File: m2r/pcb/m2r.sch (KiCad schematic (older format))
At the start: 106 parts, among them IC1 ADP3338, IC10 STM32F303C, IC11 TPS76327, IC2 APU1205-HF-3, IC3 ADuM1201, IC4 MS5611-01BA03, IC5 ADuM1201, IC6 ADL5324, IC7 NTX2B, IC8 MAX-7Q, IC9 ALM-2712, P1 CONN_2, P2 CONN_2, P3 CONN_4, P4 RockBLOCK, P5 SWD, P6 SMA, P7 CONN_2, X1 BAT BOX, X2 ARM SW, X3 RG LED, X4 8M

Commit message: add farnell number for new barometer
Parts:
- IC4: Farnell (none) -> 2362662
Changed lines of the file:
@@
 F 2 "" H 4950 1050 60  0000 C CNN
 F 3 "" H 4950 1050 60  0000 C CNN
+F 4 "2362662" H 4950 1050 60  0001 C CNN "Farnell"
 	1    4950 1050
 	1    0    0    -1

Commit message: update farnell codes
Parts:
- IC1: Farnell (none) -> 1651284
- IC10: Farnell (none) -> 2333361
- IC11: Farnell (none) -> 1755502
- IC9: Farnell (none) -> 1865153
- P4: Farnell (none) -> 1756828

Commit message: make a good start on m2d schematic
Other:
- note added: "INTERNAL STATUS LEDS"
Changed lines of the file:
@@
 Wire Wire Line
 	6000 1450 6000 1400
+Text Notes 8400 5450 0    60   ~ 0
+INTERNAL STATUS LEDS
 $EndSCHEMATC

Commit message: further wibbling about things
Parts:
- removed C4: 100n, 0603, symbol C
- removed IC2: APU1205-HF-3, symbol APU1205-HF-3
- removed IC4: MS5611-01BA03, symbol MS5611-01BA03
- removed IC7: NTX2B, symbol NTX2B
- removed R1: 10k, 0603, symbol R
- removed TP19, TP20, TP21, TP22: TESTPAD, symbol TESTPAD
- added IC2: ADP3335, symbol ADP3335
- added IC6: MTX2, symbol MTX2
- added TP13, TP14: TESTPAD, symbol TESTPAD
- renumbered C11 to C10, C12 to C11, C13 to C12, C14 to C13, C15 to C14, C16 to C15, C17 to C16, C18 to C17, C19 to C18, C20 to C19, C21 to C20, C22 to C21, C23 to C22, C24 to C23, C25 to C24, C26 to C25, C27 to C26, C28 to C27, C29 to C28, C30 to C29, C31 to C30, C32 to C31, C33 to C32, C34 to C33, C35 to C34, C5 to C4, C6 to C5, C7 to C6, C8 to C7, C9 to C8, C10 to C9, IC11 to IC10, IC5 to IC4, IC6 to IC5, IC8 to IC7, IC9 to IC8, IC10 to IC9, R2 to R1, R11 to R10, R12 to R11, R13 to R12, R14 to R13, R15 to R14, R3 to R2, R4 to R3, R5 to R4, R6 to R5, R7 to R6, R8 to R7, R9 to R8, R10 to R9, TP13 to TP15, TP14 to TP16, TP15 to TP17, TP16 to TP18, TP17 to TP19, TP18 to TP20
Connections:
- net labels added: NTX2B_P0, NTX2B_P1
- net labels removed: BARO_CS, BARO_MISO, BARO_MOSI, BARO_SCK
- wire segments 326 -> 312
- no-connect marks 24 -> 26
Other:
- note removed: "BAROMETER"
- moved on the sheet: C1, C10, C16, C2, C3, C4, C5, C9, IC3, IC4, P1, P2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

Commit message: something went weird with mtx2 footprint, redo
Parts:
- removed IC6: MTX2, symbol MTX2
- added IC?: MTX2, symbol MTX2
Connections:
- net +3.3V: now also IC?.3 (VCC)
- net GND: now also IC?.2 (GND), IC?.8 (GND)
- net NTX2B_EN: now also IC?.4 (EN/PGM)
- net NTX2B_P0: now also IC?.7 (P0)
- net NTX2B_P1: now also IC?.6 (P1)
- net NTX2B_TXD: now also IC?.5 (TXD)
- net at GS1.2 (G2): now also IC?.1 (RF)
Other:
- moved on the sheet: C16
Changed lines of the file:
@@
 L GND #PWR033
 U 1 1 537B4925
-P 5850 2650
-F 0 "#PWR033" H 5850 2650 30  0001 C CNN
-F 1 "GND" H 5850 2580 30  0001 C CNN
-F 2 "" H 5850 2650 60  0000 C CNN
-F 3 "" H 5850 2650 60  0000 C CNN
-	1    5850 2650
+P 5900 2650
+F 0 "#PWR033" H 5900 2650 30  0001 C CNN
+F 1 "GND" H 5900 2580 30  0001 C CNN
+F 2 "" H 5900 2650 60  0000 C CNN
+F 3 "" H 5900 2650 60  0000 C CNN
+	1    5900 2650
 	1    0    0    -1
 $EndComp
@@
 L C C16
 U 1 1 537B897D
-P 5300 2300
-F 0 "C16" H 5300 2400 40  0000 L CNN
-F 1 "100n" H 5306 2215 40  0000 L CNN
-F 2 "0603" H 5338 2150 30  0001 C CNN
-F 3 "" H 5300 2300 60  0000 C CNN
-F 4 "1759037" H 5300 2300 60  0001 C CNN "Farnell"
-	1    5300 2300
+P 5300 2250
+F 0 "C16" H 5300 2350 40  0000 L CNN
+F 1 "100n" H 5306 2165 40  0000 L CNN
+F 2 "0603" H 5338 2100 30  0001 C CNN
+F 3 "" H 5300 2250 60  0000 C CNN
+F 4 "1759037" H 5300 2250 60  0001 C CNN "Farnell"
+	1    5300 2250
 	0    -1   -1   0
 $EndComp
@@
 L GND #PWR066
 U 1 1 537E9BA7
-P 5550 2350
-F 0 "#PWR066" H 5550 2350 30  0001 C CNN
-F 1 "GND" H 5550 2280 30  0001 C CNN
-F 2 "" H 5550 2350 60  0000 C CNN
-F 3 "" H 5550 2350 60  0000 C CNN
-	1    5550 2350
+P 5550 2300
+F 0 "#PWR066" H 5550 2300 30  0001 C CNN
+F 1 "GND" H 5550 2230 30  0001 C CNN
+F 2 "" H 5550 2300 60  0000 C CNN
+F 3 "" H 5550 2300 60  0000 C CNN
+	1    5550 2300
 	1    0    0    -1
 $EndComp
@@
 $EndComp
 Wire Wire Line
-	4850 2300 4850 2500
+	4850 2250 4850 2500
 Connection ~ 10000 2950
 Wire Wire Line
@@
 	4750 2600 4900 2600
 Wire Wire Line
-	5500 2300 5550 2300
-Wire Wire Line
-	5550 2300 5550 2350
-Wire Wire Line
-	5100 2300 4850 2300
+	5500 2250 5550 2250
+Wire Wire Line
+	5550 2250 5550 2300
+Wire Wire Line
+	5100 2250 4850 2250
 Wire Wire Line
 	4750 2350 4850 2350
@@
 NoConn ~ 3150 5900
 NoConn ~ 3150 6000
-$Comp
-L MTX2 IC6
-U 1 1 53CAB488
-P 5350 2750
-F 0 "IC6" H 5100 3100 60  0000 C CNN
-F 1 "MTX2" H 5150 2400 60  0000 C CNN
-F 2 "" H 5350 2750 60  0000 C CNN
-F 3 "" H 5350 2750 60  0000 C CNN
-	1    5350 2750
-	1    0    0    -1
-$EndComp
 Wire Wire Line
 	4900 3000 4850 3000
-Wire Wire Line
-	5800 2600 5850 2600
-Wire Wire Line
-	5850 2600 5850 2650
 $Comp
 L GND #PWR076
@@
 $EndComp
 Connection ~ 4850 3000
-Wire Wire Line
-	5800 2500 6050 2500
 Wire Wire Line
 	6050 2500 6050 2800
@@
 Connection ~ 3300 3350
 Connection ~ 3300 3450
+$Comp
+L MTX2 IC?
+U 1 1 53CBCC8C
+P 4900 2500
+F 0 "IC?" H 5600 2600 60  0000 C CNN
+F 1 "MTX2" H 5150 2600 60  0000 C CNN
+F 2 "" H 4900 2500 60  0000 C CNN
+F 3 "" H 4900 2500 60  0000 C CNN
+	1    4900 2500
+	1    0    0    -1
+$EndComp
+Wire Wire Line
+	5850 2600 5900 2600
+Wire Wire Line
+	5900 2600 5900 2650
+Wire Wire Line
+	5850 2500 6050 2500
 $EndSCHEMATC

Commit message: reannotate m2r
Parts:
- gave numbers to parts that had none: 1
- renumbered C16 to C13, C13 to C14, C14 to C15, C15 to C16, IC5 to IC6

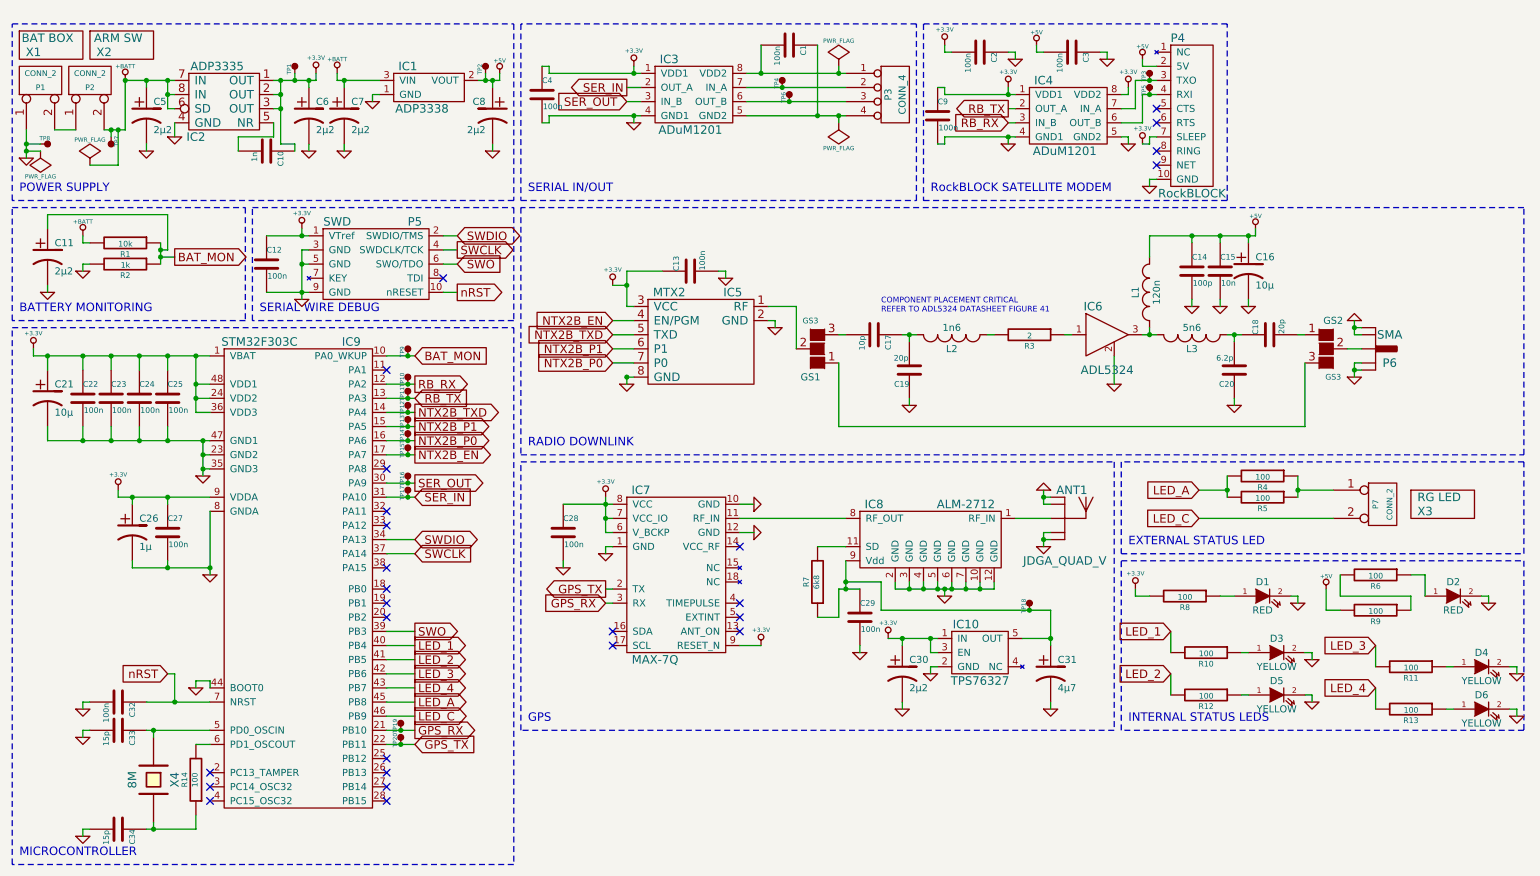
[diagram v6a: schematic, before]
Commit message: swap to JST PA range connectors
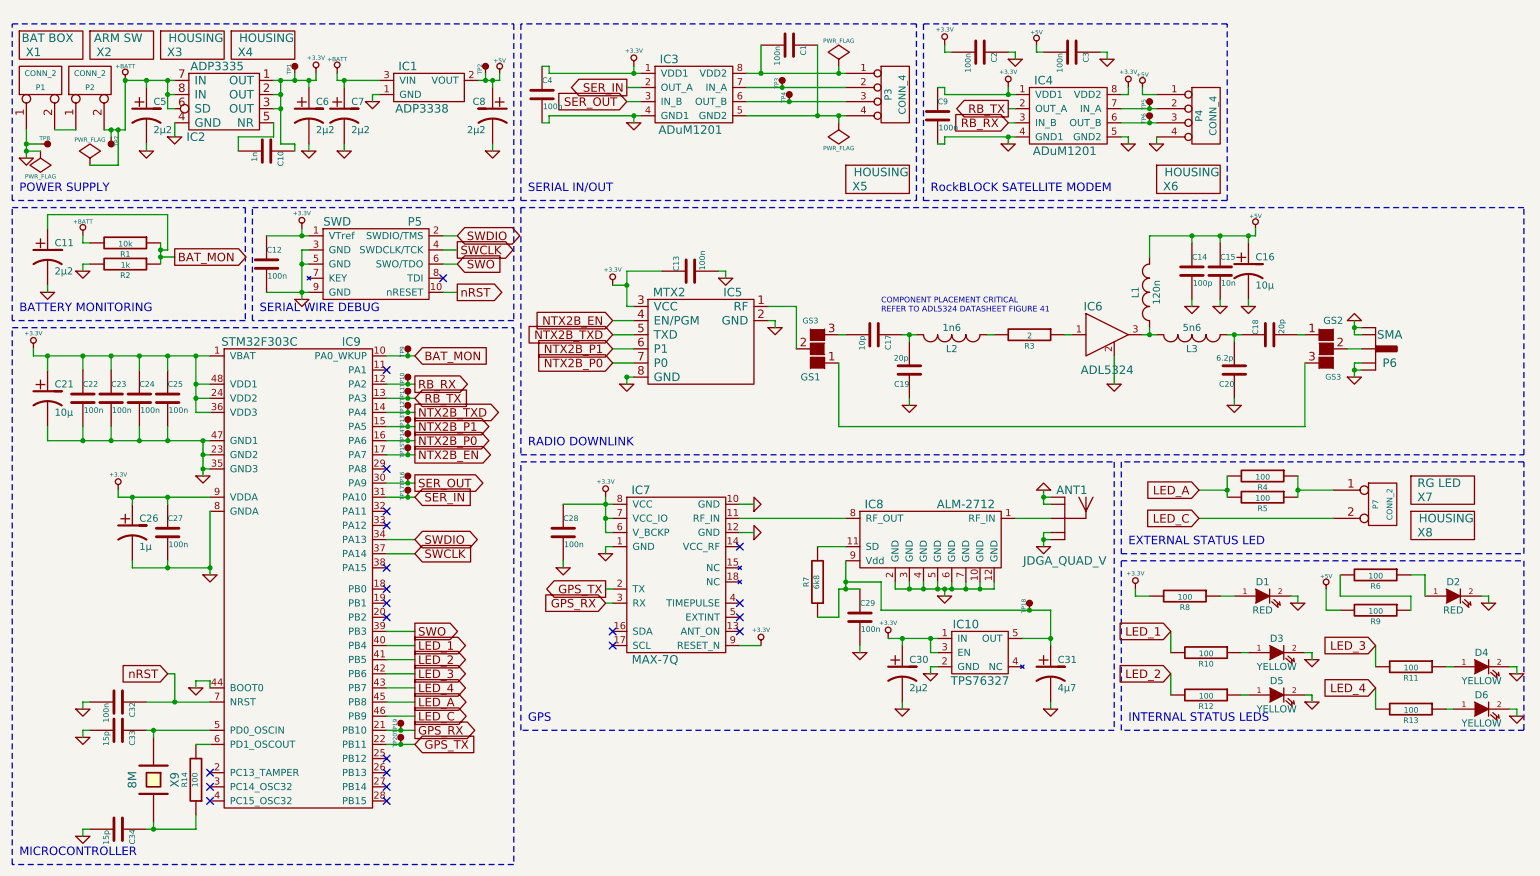
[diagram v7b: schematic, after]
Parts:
- removed P4: RockBLOCK, symbol RockBLOCK
- added P4: CONN_4, symbol CONN_4
- added X3, X4, X5, X6, X8: HOUSING, symbol PART
- C1, C10, C11, C12, C13, C15, C2, C21, C22, C23, C24, C25, C26, C27, C28, C29, C3, C30, C31, C32, C33, C34, C4, C5, C6, C7, C8, C9, D1, D2, D3, D4, D5, D6, L1, L2: footprint 0603 -> Capacitors_SMD:c_0603
- IC1: footprint (none) -> SMD_Packages:SOT223
- IC2: footprint (none) -> Housings_SSOP:MSOP-8
- IC3, IC4: footprint (none) -> Housings_SOIC:SOIC-8_N
- P1, P2, P7: Farnell 1462926 -> 1830747
- P3: Farnell 1462920 -> (none); RS (none) -> 512-8484
- R1, R10, R11, R12, R13, R14, R2, R4, R5, R6, R7, R8, R9: footprint 0603 -> SMD_Packages:SM0603_Resistor
- renumbered TP4 to TP3, TP6 to TP4, TP3 to TP5, TP5 to TP6, X3 to X7, X4 to X9
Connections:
- net +5V: now also P4.1 (P1)
- net GND: now also P4.4 (P4)
- net at IC4.7 (IN_A), TP5.1 (TP): now also P4.2 (P2)
- net at IC4.6 (OUT_B), TP6.1 (TP): now also P4.3 (P3)
- no-connect marks 26 -> 22
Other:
- moved on the sheet: TP5, TP6, X7

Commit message: rejig m2r schematic a little for i2c gps
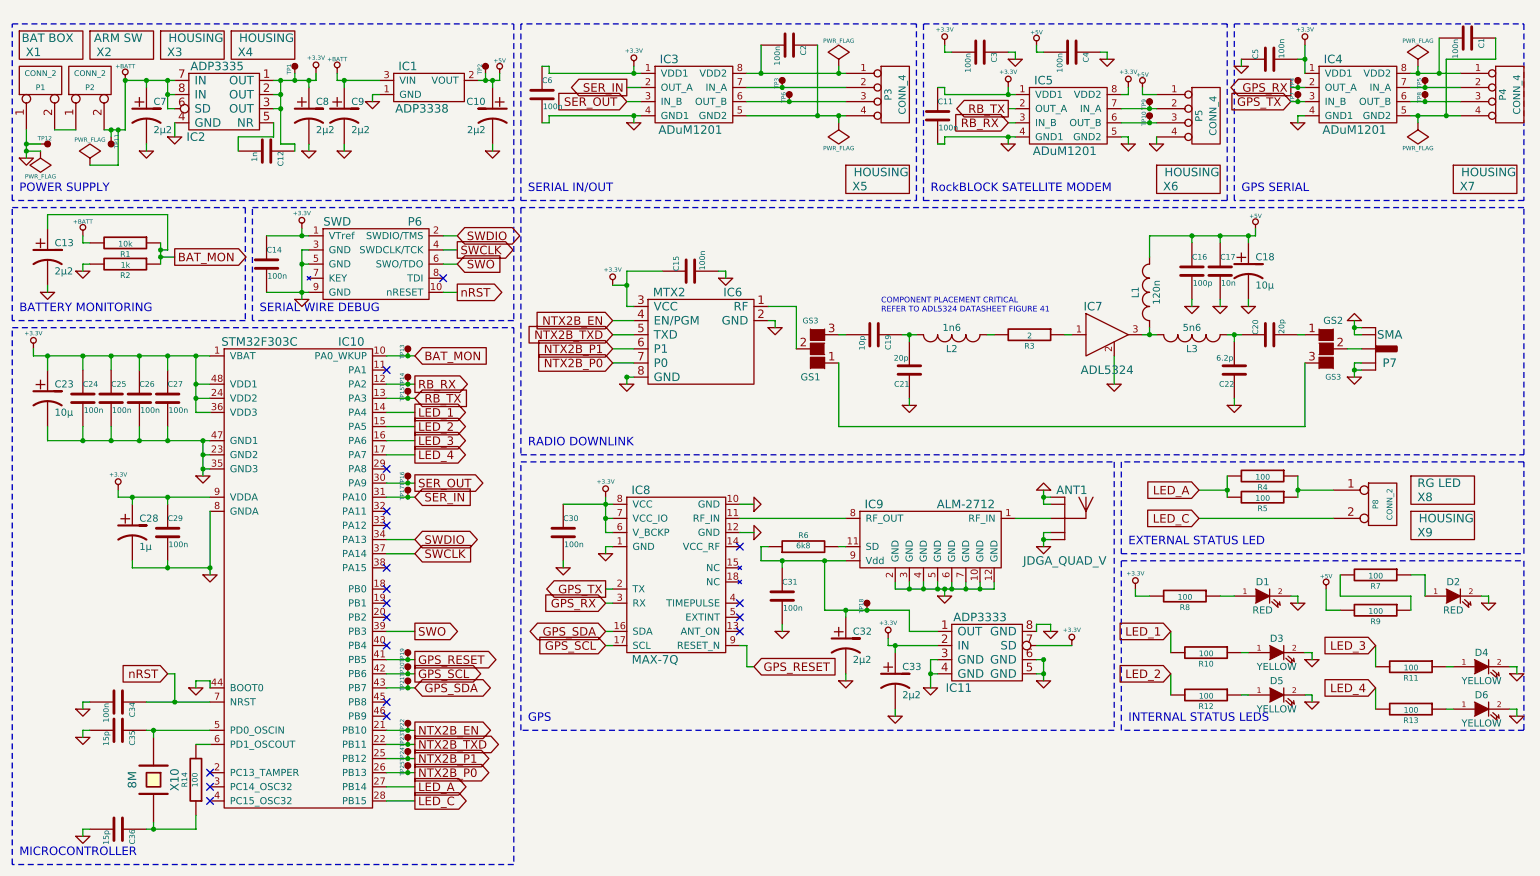
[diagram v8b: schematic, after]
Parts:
- removed C31: 4µ7, Capacitors_SMD:c_0603, symbol CP1
- removed IC10: TPS76327, symbol TPS76327
- added C1, C5: 100n, Capacitors_SMD:c_0603, symbol C
- added C32: 2µ2, Capacitors_SMD:c_0603, symbol CP1
- added IC11: ADP3333, symbol ADP3333
- added IC4: ADuM1201, Housings_SOIC:SOIC-8_N, symbol ADuM1201
- added P4: CONN_4, JST_PA:S04B-PASK-2, symbol CONN_4
- added TP21, TP4, TP5, TP7, TP8: TESTPAD, Measurement_Points:Measurement_Point_Round-SMD-Pad_Small, symbol TESTPAD
- added X7: HOUSING, symbol PART
- C16: renamed from C14; footprint 0402 -> Capacitors_SMD:c_0402
- C18: renamed from C16; footprint 1206 -> Capacitors_SMD:c_1206
- C19: renamed from C17; footprint 0402 -> Capacitors_SMD:c_0402
- C20: renamed from C18; footprint 0402 -> Capacitors_SMD:c_0402
- C21: renamed from C19; footprint 0402 -> Capacitors_SMD:c_0402
- C22: renamed from C20; footprint 0402 -> Capacitors_SMD:c_0402
- GS1, GS2: footprint GS3 -> Connect:GS3
- IC10: renamed from IC9; footprint (none) -> Housings_QFP:lqfp-48
- IC7: renamed from IC6; footprint (none) -> Housings_SOT-89:SOT89-3_Housing
- L1, L2: footprint Capacitors_SMD:c_0603 -> SMD_Packages:SM0603
- L3: footprint 0402 -> SMD_Packages:SM0402
- P1, P2: footprint (none) -> JST_PA:S02B-PASK-2
- P3: footprint (none) -> JST_PA:S04B-PASK-2
- P5: renamed from P4; footprint (none) -> JST_PA:S04B-PASK-2
- P6: renamed from P5; Farnell 1667759 -> 2308436
- P8: renamed from P7; footprint (none) -> JST_PA:S02B-PASK-2
- R3: footprint 0402 -> SMD_Packages:SM0402_r
- TP1, TP16, TP17, TP18, TP19, TP2, TP20, TP3: footprint (none) -> Measurement_Points:Measurement_Point_Round-SMD-Pad_Small
- TP10: renamed from TP6; footprint (none) -> Measurement_Points:Measurement_Point_Round-SMD-Pad_Small
- TP11: renamed from TP7; footprint (none) -> Measurement_Points:Measurement_Point_Round-SMD-Pad_Small
- TP12: renamed from TP8; footprint (none) -> Measurement_Points:Measurement_Point_Round-SMD-Pad_Small
- TP13: renamed from TP9; footprint (none) -> Measurement_Points:Measurement_Point_Round-SMD-Pad_Small
- TP14: renamed from TP10; footprint (none) -> Measurement_Points:Measurement_Point_Round-SMD-Pad_Small
- TP15: renamed from TP11; footprint (none) -> Measurement_Points:Measurement_Point_Round-SMD-Pad_Small
- TP22: renamed from TP12; footprint (none) -> Measurement_Points:Measurement_Point_Round-SMD-Pad_Small
- TP23: renamed from TP13; footprint (none) -> Measurement_Points:Measurement_Point_Round-SMD-Pad_Small
- TP24: renamed from TP14; footprint (none) -> Measurement_Points:Measurement_Point_Round-SMD-Pad_Small
- TP25: renamed from TP15; footprint (none) -> Measurement_Points:Measurement_Point_Round-SMD-Pad_Small
- TP6: renamed from TP4; footprint (none) -> Measurement_Points:Measurement_Point_Round-SMD-Pad_Small
- TP9: renamed from TP5; footprint (none) -> Measurement_Points:Measurement_Point_Round-SMD-Pad_Small
- X10: renamed from X9; footprint HC49/S -> Crystals:Crystal_HC49-U_Vertical
- renumbered C8 to C10, C9 to C11, C10 to C12, C11 to C13, C12 to C14, C13 to C15, C15 to C17, C1 to C2, C21 to C23, C22 to C24, C23 to C25, C24 to C26, C25 to C27, C26 to C28, C27 to C29, C2 to C3, C28 to C30, C29 to C31, C30 to C33, C32 to C34, C33 to C35, C34 to C36, C3 to C4, C4 to C6, C5 to C7, C6 to C8, C7 to C9, IC4 to IC5, IC5 to IC6, IC7 to IC8, IC8 to IC9, P6 to P7, R7 to R6, R6 to R7, X7 to X8, X8 to X9
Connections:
- net +3.3V: now also C5.2, IC11.2 (IN), IC11.7 (SD), IC4.1 (VDD1); no longer IC8.9 (RESET_N)
- net GND: now also C32.2, C5.1, IC11.3 (GND), IC11.4 (GND), IC11.5 (GND), IC11.6 (GND), IC11.8 (GND), IC4.4 (GND1)
- net GPS_RX: now also IC4.2 (OUT_A), TP4.1 (TP); no longer IC10.21 (PB10), TP19.1 (TP)
- net GPS_TX: now also IC4.3 (IN_B), TP7.1 (TP); no longer IC10.22 (PB11), TP20.1 (TP)
- net LED_1: now also IC10.14 (PA4); no longer IC10.40 (PB4)
- net LED_2: now also IC10.15 (PA5); no longer IC10.41 (PB5)
- net LED_3: now also IC10.16 (PA6); no longer IC10.42 (PB6)
- net LED_4: now also IC10.17 (PA7); no longer IC10.43 (PB7)
- net LED_A: now also IC10.27 (PB14); no longer IC10.45 (PB8)
- net LED_C: now also IC10.28 (PB15); no longer IC10.46 (PB9)
- net NTX2B_EN: now also IC10.21 (PB10), TP22.1 (TP); no longer IC10.17 (PA7), TP25.1 (TP)
- net NTX2B_P0: now also IC10.26 (PB13), TP25.1 (TP); no longer IC10.16 (PA6), TP24.1 (TP)
- net NTX2B_P1: now also IC10.25 (PB12), TP24.1 (TP); no longer IC10.15 (PA5), TP23.1 (TP)
- net NTX2B_TXD: now also IC10.22 (PB11), TP23.1 (TP); no longer IC10.14 (PA4), TP22.1 (TP)
- net GPS_SDA: now reaches IC8.16 (SDA)
- net GPS_SDA: now also IC10.43 (PB7), TP21.1 (TP)
- net GPS_SCL: now reaches IC8.17 (SCL)
- net GPS_SCL: now also IC10.42 (PB6), TP20.1 (TP)
- net at C31.1, IC9.9 (Vdd), R6.1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: now also C32.1, IC11.1 (OUT)
- new net: C1.1, IC4.5 (GND2), P4.4 (P4)
- new net: IC4.6 (OUT_B), P4.3 (P3), TP8.1 (TP)
- new net: IC4.7 (IN_A), P4.2 (P2), TP5.1 (TP)
- new net: C1.2, IC4.8 (VDD2), P4.1 (P1)
- new net GPS_RESET: IC10.41 (PB5), IC8.9 (RESET_N), TP19.1 (TP)
- no-connect marks 22 -> 19
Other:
- note added: "GPS SERIAL"
- moved on the sheet: C31, C33, R6, TP18, TP22, TP23, TP24, TP25
